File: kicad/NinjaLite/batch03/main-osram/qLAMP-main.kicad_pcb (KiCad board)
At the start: 2 copper layers, 142 x 58 mm, 119 parts, among them J1 ALI_USB, J13 Conn_01x01_Male, J16 Conn_01x01_Male, J2 Barrel_Jack_Switch, J23 Conn_01x01_Male, J24 Conn_01x02_Male, J25 Conn_01x02_Male, J26 Conn_01x02_Male, J27 Conn_01x02_Male, J3 Conn_01x07_Male, J4 Conn_01x02_Male, J5 Conn_01x01_Male, J6 Conn_01x01_Male, J7 Conn_01x01_Male, Q1 Q_NMOS_GSD, Q3 Q_NMOS_GSD, Q5 Q_NMOS_GSD, U1 NAU7802, U10 TLC5929, U11 IP2721, U14 TCR3DF33,LM(CT, U17 LITE_LCD, U19 CD74HC4067M96, U2 NAU7802, U3 BD433M5FP-CE2, U4 LMP7717MF_NOPB, U5 ESP32-WROOM-32, U6 BA178M05FP-E2, U8 TS12A12511DCNR, U9 SN74LV4051A

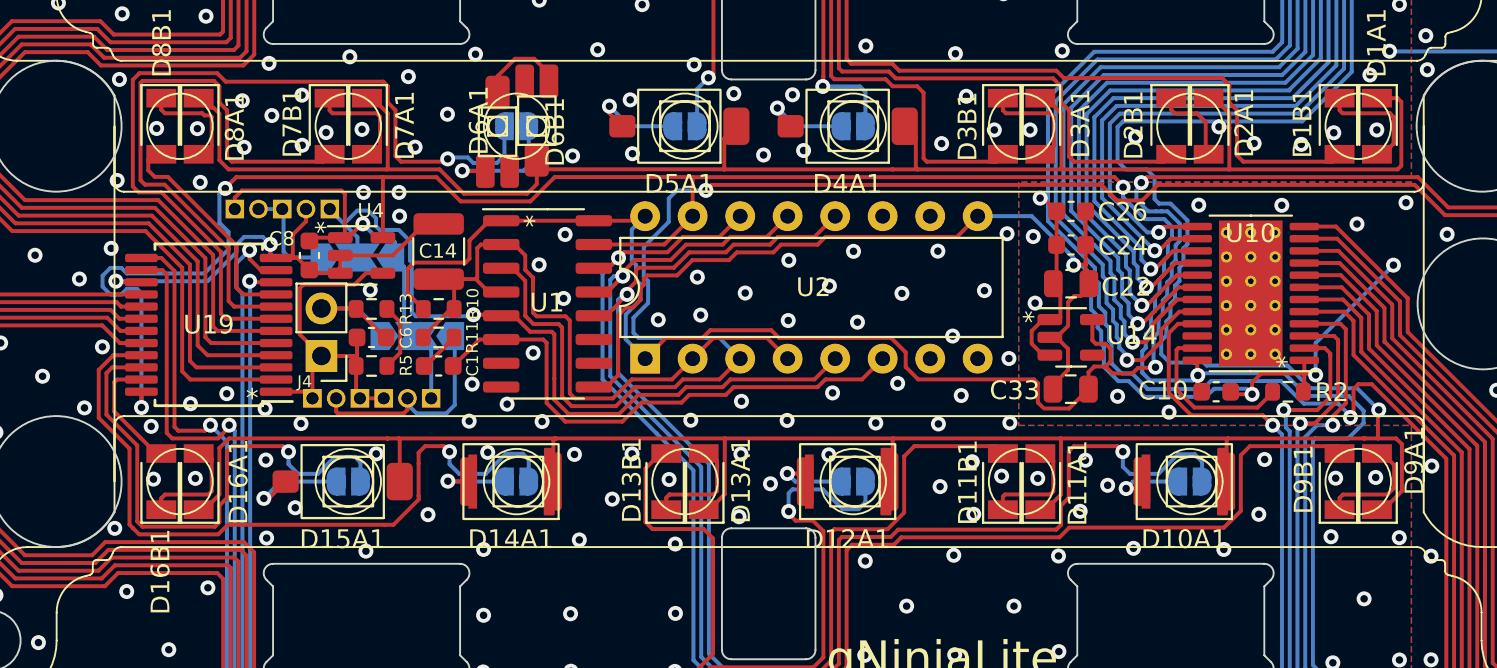
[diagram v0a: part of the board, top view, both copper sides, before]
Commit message: add pads below all pds
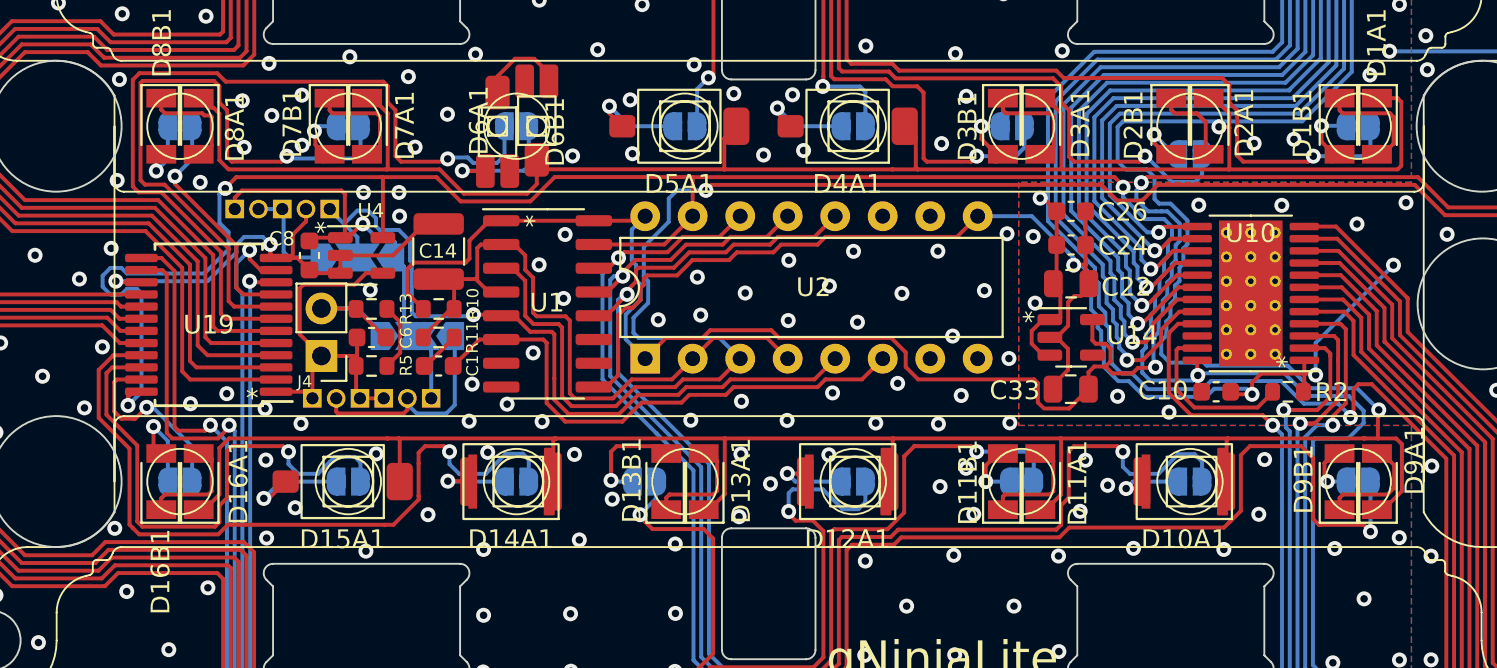
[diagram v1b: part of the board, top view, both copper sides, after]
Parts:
- added JP14: Jumper_2_Open, Jumper:SolderJumper-2_P1.3mm_Open_RoundedPad1.0x1.5mm, B.Cu at (144.2, 92.5)
- added JP15: Jumper_2_Open, Jumper:SolderJumper-2_P1.3mm_Open_RoundedPad1.0x1.5mm, B.Cu at (135.2, 94.0)
- added JP16: Jumper_2_Open, Jumper:SolderJumper-2_P1.3mm_Open_RoundedPad1.0x1.5mm, B.Cu at (125.7, 92.5)
- added JP17: Jumper_2_Open, Jumper:SolderJumper-2_P1.3mm_Open_RoundedPad1.0x1.5mm, B.Cu at (90.2, 92.5)
- added JP18: Jumper_2_Open, Jumper:SolderJumper-2_P1.3mm_Open_RoundedPad1.0x1.5mm, B.Cu at (81.2, 92.5)
- added JP19: Jumper_2_Open, Jumper:SolderJumper-2_P1.3mm_Open_RoundedPad1.0x1.5mm, B.Cu at (144.2, 111.5)
- added JP20: Jumper_2_Open, Jumper:SolderJumper-2_P1.3mm_Open_RoundedPad1.0x1.5mm, B.Cu at (126.2, 111.5)
- added JP21: Jumper_2_Open, Jumper:SolderJumper-2_P1.3mm_Open_RoundedPad1.0x1.5mm, B.Cu at (106.0, 111.5)
- added JP22: Jumper_2_Open, Jumper:SolderJumper-2_P1.3mm_Open_RoundedPad1.0x1.5mm, B.Cu at (81.2, 111.5)
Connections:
- D11B1 pad 2: /PhotoMUX/S_PD_OUT5 -> Net-(D11B1-Pad2)
- D13B1 pad 2: /PhotoMUX/S_PD_OUT9 -> Net-(D13B1-Pad2)
- D16B1 pad 2: /PhotoMUX/S_PD_OUT15 -> Net-(D16B1-Pad2)
- D1B1 pad 2: /PhotoMUX/N_PD_OUT1 -> Net-(D1B1-Pad2)
- D2B1 pad 2: /PhotoMUX/N_PD_OUT3 -> Net-(D2B1-Pad2)
- D3B1 pad 2: /PhotoMUX/N_PD_OUT5 -> Net-(D3B1-Pad2)
- D7B1 pad 2: /PhotoMUX/N_PD_OUT13 -> Net-(D7B1-Pad2)
- D8B1 pad 2: /PhotoMUX/N_PD_OUT15 -> Net-(D8B1-Pad2)
- D9B1 pad 2: /PhotoMUX/S_PD_OUT1 -> Net-(D9B1-Pad2)
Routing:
- net /PhotoMUX/S_PD_OUT1: track 116.4 -> 123.6 mm, vias 0 -> 1
- net Net-(D13B1-Pad2): track 0.00 -> 6.25 mm, vias 0 -> 1
- net Net-(D16B1-Pad2): track 0.00 -> 5.14 mm, vias 0 -> 1
- net Net-(D3B1-Pad2): track 0.00 -> 4.27 mm, vias 0 -> 1
- net Net-(D9B1-Pad2): track 0.00 -> 4.07 mm, vias 0 -> 1
- net Net-(D8B1-Pad2): track 0.00 -> 4.03 mm, vias 0 -> 1
- net Net-(D1B1-Pad2): track 0.00 -> 3.98 mm, vias 0 -> 1
- net /PhotoMUX/S_PD_OUT15: track 6.53 -> 10.4 mm, vias 0 -> 1
- net Net-(D2B1-Pad2): track 0.00 -> 3.86 mm, vias 0 -> 1
- net Net-(D7B1-Pad2): track 0.00 -> 3.52 mm, vias 0 -> 1
- net /PhotoMUX/N_PD_OUT3: track 113.9 -> 117.3 mm, vias 0 -> 1
- net Net-(D11B1-Pad2): track 0.00 -> 3.31 mm, vias 0 -> 1
- net /PhotoMUX/N_PD_OUT13: track 31.0 -> 34.2 mm, vias 0 -> 1
- net /PhotoMUX/S_PD_OUT5: track 95.5 -> 98.4 mm, vias 0 -> 1
- net /PhotoMUX/N_PD_OUT1: track 124.5 -> 127.5 mm, vias 0 -> 1
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
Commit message: wiring batch04/main
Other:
- board text added: "V(IC,SEL,SELP) must be one of them. V(IP2721|IP2721_D,High,Floating)=20 V(IP2721|IP2721_D,F,F)=15 V(IP2721|IP2721_D,Low,F)=5 V(IP2721_D,F,H)=12 V(IP2721_D,F,L)=9 V(IP2721_MAX12,H,F)=12 V(IP2721_MAX12,F,F)=9 V(IP2721_MAX12,L,F)=5"
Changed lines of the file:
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@@
     (effects (font (size 1 1) (thickness 0.15)))
+  )
+  (gr_text "V(IC,SEL,SELP) must be one of them.\nV(IP2721|IP2721_D,High,Floating)=20\nV(IP2721|IP2721_D,F,F)=15\nV(IP2721|IP2721_D,Low,F)=5\nV(IP2721_D,F,H)=12\nV(IP2721_D,F,L)=9\nV(IP2721_MAX12,H,F)=12\nV(IP2721_MAX12,F,F)=9\nV(IP2721_MAX12,L,F)=5" (at 185.79 60.56) (layer "F.SilkS")
+    (effects (font (size 1 1) (thickness 0.25)) (justify left))
   )
   (gr_text "*" (at 85.02 107.04) (layer "F.SilkS")
